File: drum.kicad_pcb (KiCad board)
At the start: 4 copper layers, 70 x 70 mm, 112 parts, among them J1001 NE8FAV, J101 Cortex, J102 DX07S016JA3, J501 WAGO 2065-100, J502 WAGO 2065-100, J601 WAGO 2065-100, J602 WAGO 2065-100, J701 WAGO 2065-100, J702 WAGO 2065-100, J703 WAGO 2065-100, J704 WAGO 2065-100, J801 WAGO 2065-100, J802 WAGO 2065-100, J803 WAGO 2065-100, J901 NE8FAV, Q201 BSC010N04LS, Q202 BSC010N04LS, Q501 BSC010N04LS, Q601 BSC010N04LS, SW101 SKSG, SW102 SKSG, U1001 THVD2442, U101 ATSAMD51J, U102 TPS78433QWDRBRQ1, U201 LM74502-Q1, U301 TPSM33625, U401 BTT6010, U701 TMC2130-LA, U801 74AHC1G125, U901 THVD2442, Y101 32k768

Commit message: Replace diode
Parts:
- D401: value RB501SM -> PMEG2010EPK; footprint V2_Diode_SMD:D_SOD-523 -> V2_Diode_SMD:D_SOD-1608
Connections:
- net +VBUS renamed /+VBUS
- net +VLINK renamed /+VLINK
- net Shield renamed /Shield

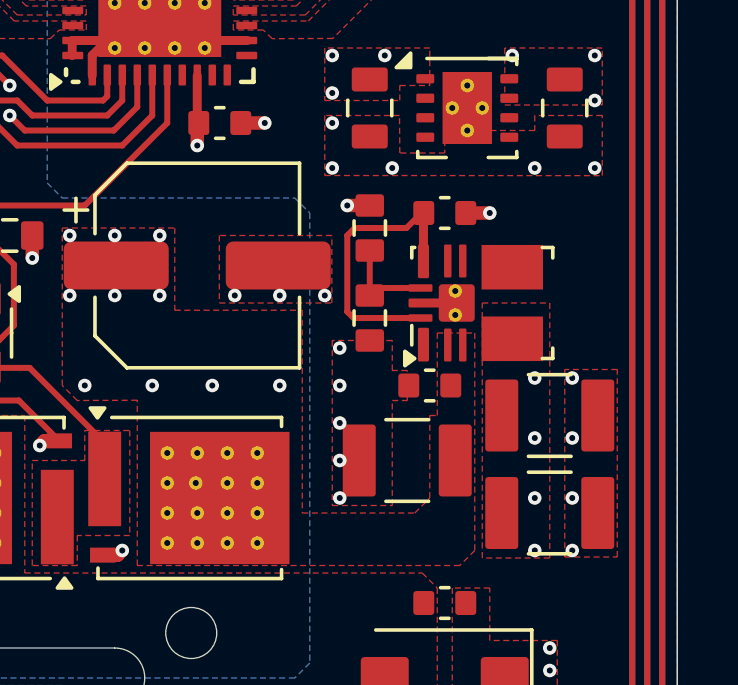
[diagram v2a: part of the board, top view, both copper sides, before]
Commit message: Replace step-down
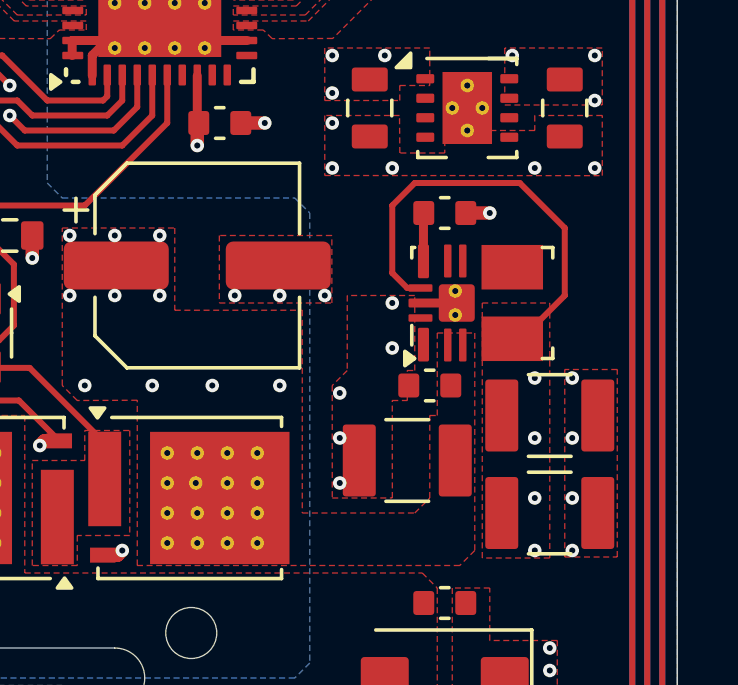
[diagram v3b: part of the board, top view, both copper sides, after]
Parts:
- removed R301: 40k2, V2_Resistor_SMD:R_0603
- removed R302: 10k, V2_Resistor_SMD:R_0603
- U301: value TPSM33625 -> TPSM33620S5QRDNRQ1
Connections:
- U301 pad 11: /Power +5V/Vcc -> GND
- U301 pad 9: /Power +5V/Feedback -> +5V
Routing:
- net +5V: track 5.42 -> 19.3 mm, vias 18 -> 17
- net /Power +5V/Vcc: track 9.49 -> 1.64 mm
- net /Power +5V/Feedback: track 3.11 -> 0.00 mm

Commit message: Update
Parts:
- renumbered C107 to C101, C108 to C102, C109 to C103, C110 to C104, C101 to C105, C102 to C106, C103 to C107, C104 to C108, C105 to C109, C106 to C110, C305 to C303, C303 to C304, C304 to C305, C404 to C401, C403 to C402, C402 to C403, C401 to C404, C706 to C701, C707 to C702, C701 to C703, C702 to C704, C708 to C705, C703 to C706, C704 to C707, C705 to C708, D102 to D101, D103 to D102, D101 to D103, ICON102 to ICON101, ICON101 to ICON102, R104 to R101, R101 to R102, R102 to R103, R103 to R104, R405 to R401, R408 to R402, R407 to R403, R409 to R404, R410 to R405, R401 to R407, R403 to R408, R404 to R409, R402 to R410, SW102 to SW101, SW101 to SW102, U102 to U101, U101 to U102
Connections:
- net /VDDCORE renamed /+VCORE

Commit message: Good Bye Imperial
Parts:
- C1001, C101, C102, C105, C106, C107, C108, C109, C110, C201, C202, C302, C303, C401, C402, C403, C404, C501, C601, C701, C702, C703, C705, C709, C901: footprint V2_Capacitor_SMD:C_0603 -> V2_Capacitor_SMD:C_1608
- C103, C104: footprint V2_Capacitor_SMD:C_0805 -> V2_Capacitor_SMD:C_2012
- C301, C304, C305, C707, C708: footprint V2_Capacitor_SMD:C_1210 -> V2_Capacitor_SMD:C_3225
- D103: footprint V2_LED:LED_0603 -> V2_LED:LED_1608
- R1001, R101, R102, R103, R104, R201, R202, R401, R402, R403, R404, R405, R406, R407, R408, R409, R410, R701, R901: footprint V2_Resistor_SMD:R_0603 -> V2_Resistor_SMD:R_1608
- R702, R703: footprint V2_Resistor_SMD:R_0805 -> V2_Resistor_SMD:R_2012
